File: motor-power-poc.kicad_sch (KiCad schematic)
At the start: 53 parts, among them J1 Conn_01x04_Pin, SW1 SW_Push, SW2 SW_Push, U1 QRE1113GR, U2 QRE1113GR, U3 QRE1113GR, U4 ESP32-S3FH4R2, Y1 48M

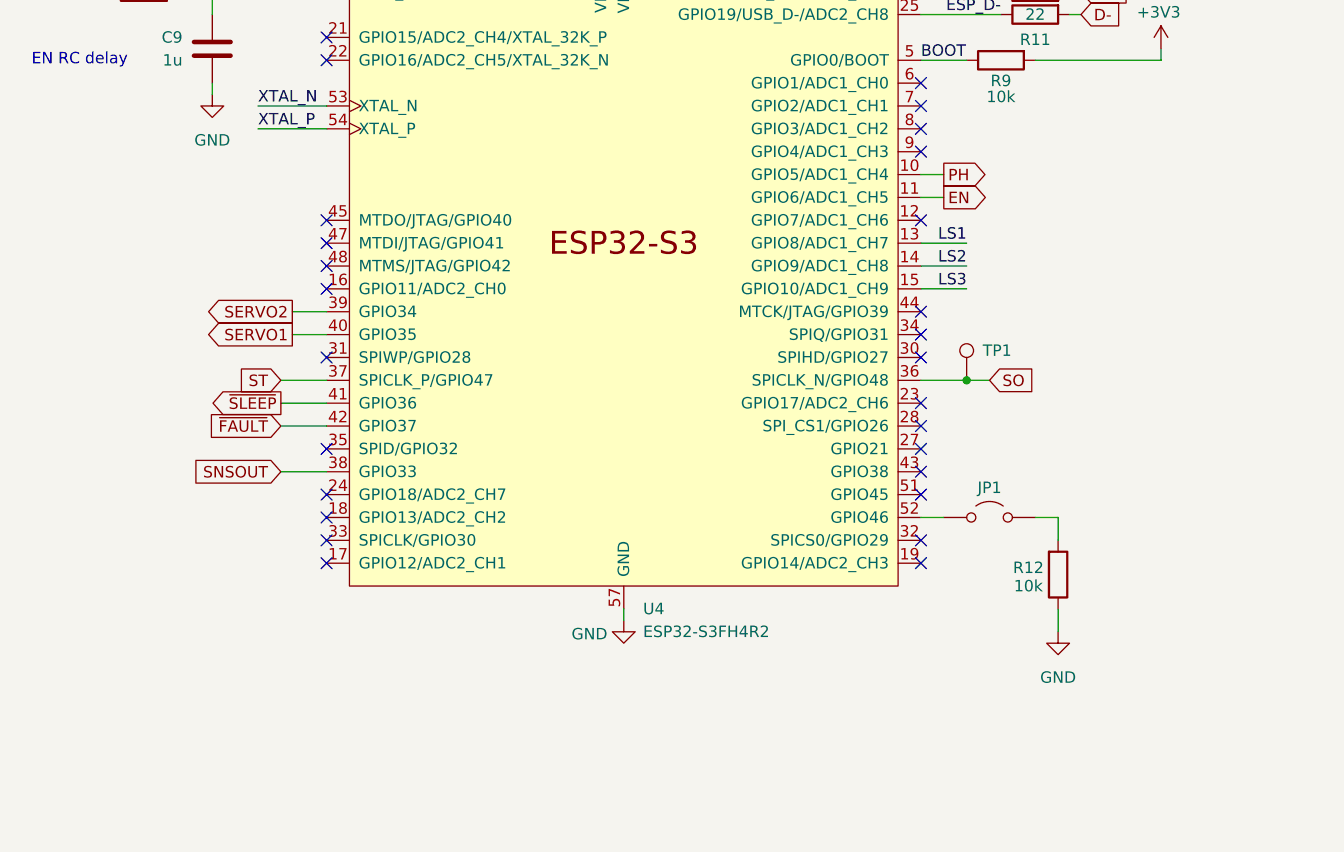
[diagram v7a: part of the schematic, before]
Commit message: schem: ESP32 pin reorganisation
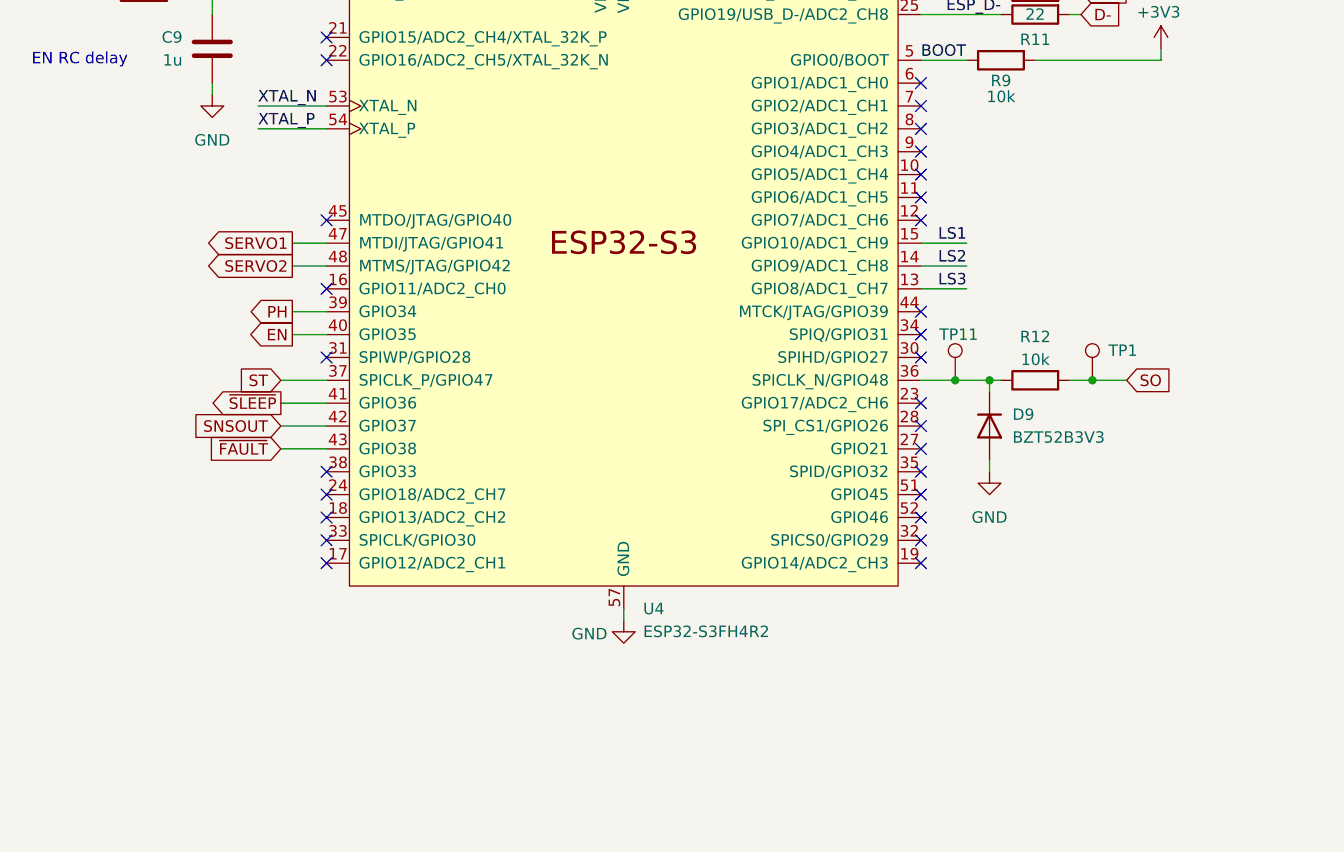
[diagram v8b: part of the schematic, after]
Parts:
- removed JP1: Jumper_2_Open, Jumper:SolderJumper-2_P1.3mm_Open_RoundedPad1.0x1.5mm, symbol Jumper:Jumper_2_Open
- added D9: BZT52B3V3, Diode_SMD:D_SOD-123, symbol Device:D
- added TP11: TestPoint, GLCS:TestPoint_Keystone_5015_Micro_Mini, symbol Connector:TestPoint
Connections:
- net EN: now also U4.40 (GPIO35); no longer U4.11 (GPIO6/ADC1_CH5)
- net GND: now also D9.2 (A); no longer R12.1
- net LS1: now also U4.15 (GPIO10/ADC1_CH9); no longer U4.13 (GPIO8/ADC1_CH7)
- net LS3: now also U4.13 (GPIO8/ADC1_CH7); no longer U4.15 (GPIO10/ADC1_CH9)
- net PH: now also U4.39 (GPIO34); no longer U4.10 (GPIO5/ADC1_CH4)
- net SERVO1: now also U4.47 (MTDI/JTAG/GPIO41); no longer U4.40 (GPIO35)
- net SERVO2: now also U4.48 (MTMS/JTAG/GPIO42); no longer U4.39 (GPIO34)
- net SNSOUT: now also U4.42 (GPIO37); no longer U4.38 (GPIO33)
- net SO: now also R12.2; no longer U4.36 (SPICLK_N/GPIO48)
- net ~{FAULT}: now also U4.43 (GPIO38); no longer U4.42 (GPIO37)
- new net: D9.1 (K), R12.1, TP11.1, U4.36 (SPICLK_N/GPIO48)
- no-connect marks 27 -> 28
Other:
- moved on the sheet: TP1
